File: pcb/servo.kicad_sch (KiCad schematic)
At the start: 13 parts, among them J3 0436500415, J4 2147511041, Q4 NTR4003N, Q5 Si3407DV

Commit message: Add MPN field for components except resistors
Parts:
- J3: MPN (none) -> 0436500415
- J4: MPN (none) -> 2147511041
- Q4: MPN (none) -> NTR4003N
- Q5: MPN (none) -> Si3407DV
- TP18, TP19, TP20, TP21, TP22: MPN (none) -> RCUCTE
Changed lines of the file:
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@@
+			)
+		)
+		(property "MPN" "RCUCTE"
+			(at 76.2 53.34 0)
+			(effects
+				(font
+					(size 1.27 1.27)
+				)
+				(hide yes)
 			)
 		)
@@
 			)
 		)
+		(property "MPN" ""
+			(at 76.2 44.45 0)
+			(effects
+				(font
+					(size 1.27 1.27)
+				)
+				(hide yes)
+			)
+		)
 		(pin "1"
 		)
@@
 		)
 		(property "Description" "test point"
+			(at 50.8 60.96 0)
+			(effects
+				(font
+					(size 1.27 1.27)
+				)
+				(hide yes)
+			)
+		)
+		(property "MPN" "RCUCTE"
 			(at 50.8 60.96 0)
 			(effects
@@
 			)
 		)
+		(property "MPN" ""
+			(at 69.85 50.8 90)
+			(effects
+				(font
+					(size 1.27 1.27)
+				)
+				(hide yes)
+			)
+		)
 		(pin "2"
 		)
@@
 			)
 		)
+		(property "MPN" ""
+			(at 44.45 63.5 90)
+			(effects
+				(font
+					(size 1.27 1.27)
+				)
+				(hide yes)
+			)
+		)
 		(pin "2"
 		)
@@
 			)
 		)
+		(property "MPN" ""
+			(at 50.8 69.85 0)
+			(effects
+				(font
+					(size 1.27 1.27)
+				)
+				(hide yes)
+			)
+		)
 		(pin "1"
 		)
@@
 			)
 		)
+		(property "MPN" "NTR4003N"
+			(at 60.96 63.5 0)
+			(effects
+				(font
+					(size 1.27 1.27)
+				)
+				(hide yes)
+			)
+		)
 		(pin "3"
 		)
@@
 			)
 		)
+		(property "MPN" "0436500415"
+			(at 137.16 54.61 0)
+			(effects
+				(font
+					(size 1.27 1.27)
+				)
+				(hide yes)
+			)
+		)
 		(pin "1"
 		)
@@
 			)
 		)
+		(property "MPN" "RCUCTE"
+			(at 101.6 60.96 0)
+			(effects
+				(font
+					(size 1.27 1.27)
+				)
+				(hide yes)
+			)
+		)
 		(pin "1"
 		)
@@
 		)
 		(property "Description" "test point"
+			(at 129.54 49.53 0)
+			(effects
+				(font
+					(size 1.27 1.27)
+				)
+				(hide yes)
+			)
+		)
+		(property "MPN" "RCUCTE"
 			(at 129.54 49.53 0)
 			(effects
@@
 			)
 		)
+		(property "MPN" "RCUCTE"
+			(at 127 43.18 0)
+			(effects
+				(font
+					(size 1.27 1.27)
+				)
+				(hide yes)
+			)
+		)
 		(pin "1"
 		)
@@
 		(property "Description" "P-Channel 20-V (D-S) MOSFET 24mOhm Rds(on) 8A Vishay Siliconix"
 			(at 86.36 29.972 0)
+			(effects
+				(font
+					(size 1.27 1.27)
+				)
+				(hide yes)
+			)
+		)
+		(property "MPN" "Si3407DV"
+			(at 86.36 50.8 0)
 			(effects
 				(font
@@
 			(at 137.16 78.74 0)
 			(effects
+				(font
+					(size 1.27 1.27)
+				)
+				(hide yes)
+			)
+		)
+		(property "MPN" "2147511041"
+			(at 137.16 78.74 0)
+			(effects

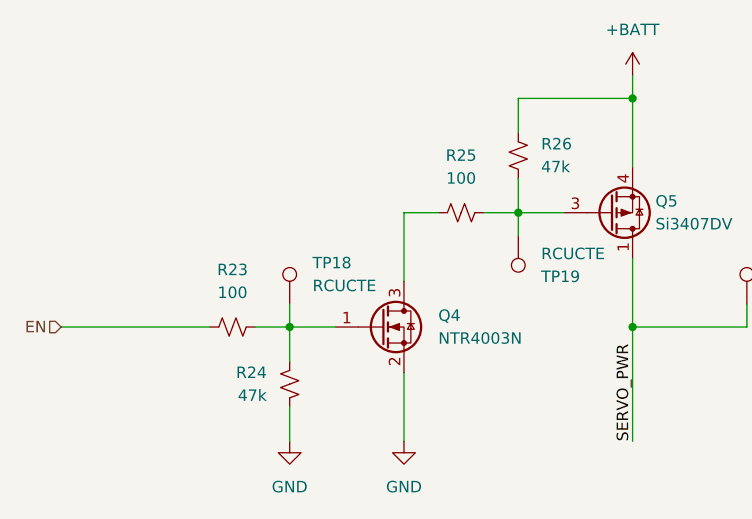
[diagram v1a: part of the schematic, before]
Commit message: BOM optimize 100 ohm resistors to 150 ohm
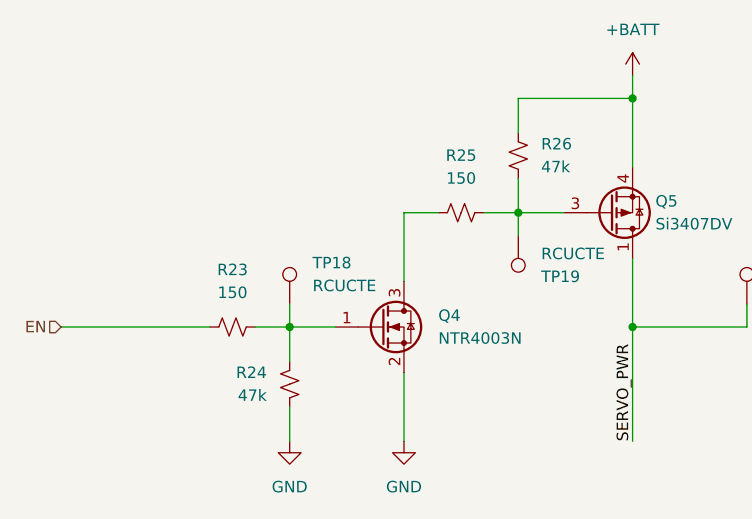
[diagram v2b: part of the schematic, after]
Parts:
- R23, R25: value 100 -> 150
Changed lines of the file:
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@@
 			)
 		)
-		(property "Value" "100"
+		(property "Value" "150"
 			(at 69.85 46.99 90)
 			(effects
@@
 			)
 		)
-		(property "Value" "100"
+		(property "Value" "150"
 			(at 44.45 59.69 90)
 			(effects

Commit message: Update resistor MPNs
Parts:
- R23, R25: MPN (none) -> RC0603JR-07150RL
- R24, R26: MPN (none) -> RC0603FR-0747KL
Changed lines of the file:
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@@
 			)
 		)
-		(property "MPN" ""
+		(property "MPN" "RC0603FR-0747KL"
 			(at 76.2 44.45 0)
 			(effects
@@
 			)
 		)
-		(property "MPN" ""
+		(property "MPN" "RC0603JR-07150RL"
 			(at 69.85 50.8 90)
 			(effects
@@
 			)
 		)
-		(property "MPN" ""
+		(property "MPN" "RC0603JR-07150RL"
 			(at 44.45 63.5 90)
 			(effects
@@
 			)
 		)
-		(property "MPN" ""
+		(property "MPN" "RC0603FR-0747KL"
 			(at 50.8 69.85 0)
 			(effects

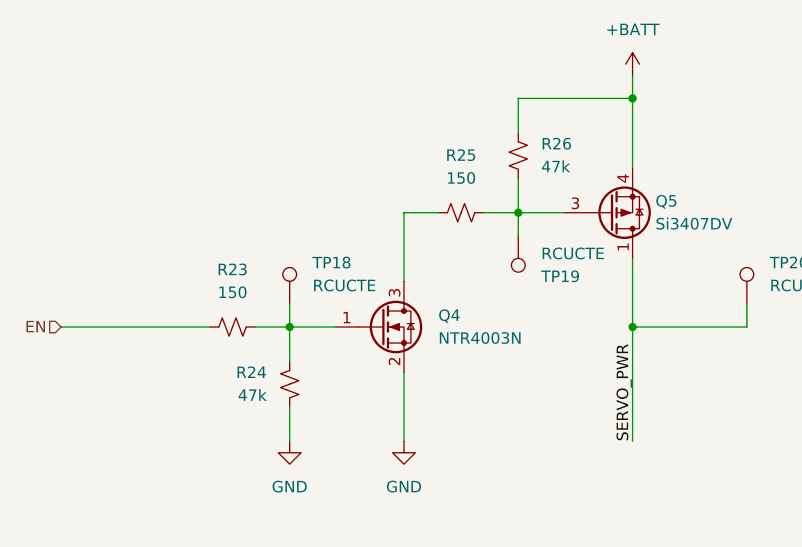
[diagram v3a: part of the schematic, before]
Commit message: Redo layout and routing for RGB LEDs
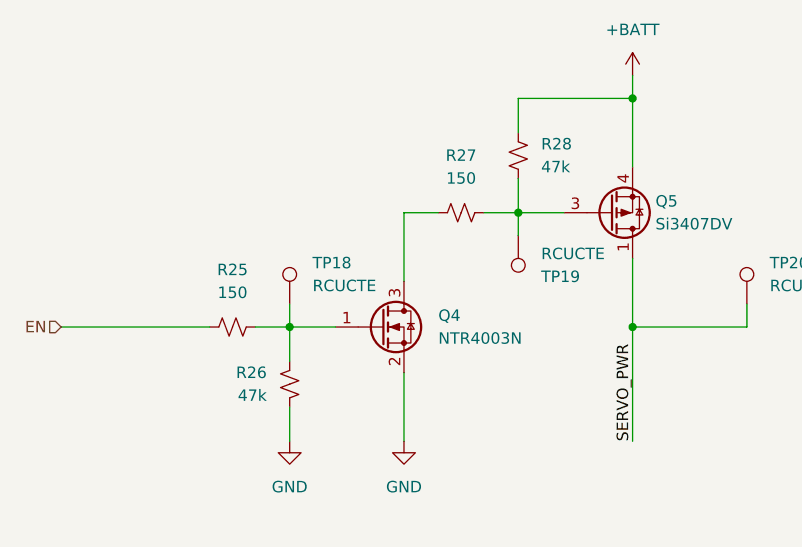
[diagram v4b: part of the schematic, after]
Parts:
- renumbered R23 to R25, R24 to R26, R25 to R27, R26 to R28
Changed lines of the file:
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@@
 		(on_board yes)
 		(dnp no)
-		(property "Reference" "R26"
+		(property "Reference" "R28"
 			(at 78.74 43.1799 0)
 			(effects
@@
 			(project ""
 				(path "/1f4fd4ed-9886-4375-a5ac-dc32d5760936/27a1e4e9-ed52-4396-b65c-2ca15ccf5a1d"
-					(reference "R26")
+					(reference "R28")
 					(unit 1)
 				)
@@
 		(dnp no)
 		(fields_autoplaced yes)
-		(property "Reference" "R25"
+		(property "Reference" "R27"
 			(at 69.85 44.45 90)
 			(effects
@@
 			(project ""
 				(path "/1f4fd4ed-9886-4375-a5ac-dc32d5760936/27a1e4e9-ed52-4396-b65c-2ca15ccf5a1d"
-					(reference "R25")
+					(reference "R27")
 					(unit 1)
 				)
@@
 		(dnp no)
 		(fields_autoplaced yes)
-		(property "Reference" "R23"
+		(property "Reference" "R25"
 			(at 44.45 57.15 90)
 			(effects
@@
 			(project "airbrake_mod"
 				(path "/1f4fd4ed-9886-4375-a5ac-dc32d5760936/27a1e4e9-ed52-4396-b65c-2ca15ccf5a1d"
-					(reference "R23")
+					(reference "R25")
 					(unit 1)
 				)
@@
 		(on_board yes)
 		(dnp no)
-		(property "Reference" "R24"
+		(property "Reference" "R26"
 			(at 48.26 68.5799 0)
 			(effects
@@
 			(project "airbrake_mod"
 				(path "/1f4fd4ed-9886-4375-a5ac-dc32d5760936/27a1e4e9-ed52-4396-b65c-2ca15ccf5a1d"
-					(reference "R24")
-					(unit 1)
-				)
+					(reference "R26")
+					(unit 1)
+				)
